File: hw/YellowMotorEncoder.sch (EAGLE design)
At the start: 20 parts, among them P1 M1

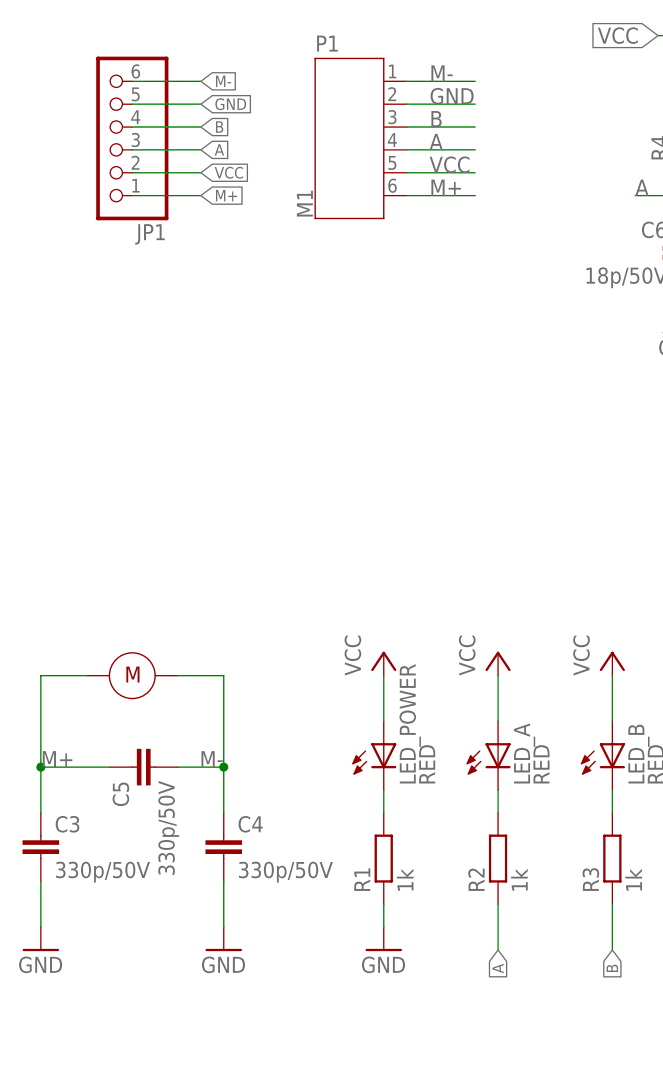
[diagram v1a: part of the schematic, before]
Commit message: Finish routing YellowMotorEncoder v1.0
- route PCB
- correct position of mounting holes
- fix connectors signal
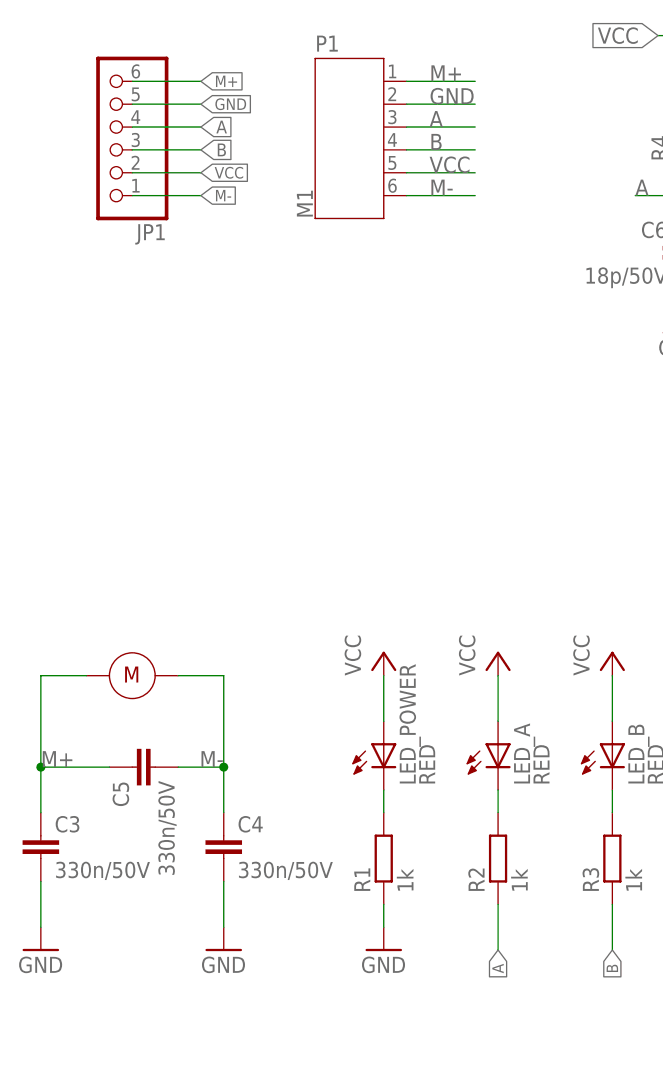
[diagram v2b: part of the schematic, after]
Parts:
- C3, C4, C5: value 330p/50V -> 330n/50V
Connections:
- net A: now also JP1.4, P1.3; no longer JP1.3, P1.4
- net B: now also JP1.3, P1.4; no longer JP1.4, P1.3
- net M+: now also JP1.6, P1.1, U$3.P$2; no longer JP1.1, P1.6, U$3.P$1
- net M-: now also JP1.1, P1.6, U$3.P$1; no longer JP1.6, P1.1, U$3.P$2
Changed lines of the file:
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@@
 <attribute name="PRICE_DATE" value="2020-05-08"/>
 </part>
-<part name="C3" library="rcl" deviceset="C-EU" device="C0805" value="330p/50V">
+<part name="C3" library="rcl" deviceset="C-EU" device="C0805" value="330n/50V">
 <attribute name="DESCRIPTION" value=" MULTILAYER CERAMIC CAPACITORS MLCC - SMD/SMT 330NF 50V 0805 ROHS"/>
 <attribute name="EXTENDED" value="NO"/>
@@
 <attribute name="PRICE_DATE" value="2020-05-08"/>
 </part>
-<part name="C4" library="rcl" deviceset="C-EU" device="C0805" value="330p/50V">
+<part name="C4" library="rcl" deviceset="C-EU" device="C0805" value="330n/50V">
 <attribute name="DESCRIPTION" value=" MULTILAYER CERAMIC CAPACITORS MLCC - SMD/SMT 330NF 50V 0805 ROHS"/>
 <attribute name="EXTENDED" value="NO"/>
@@
 <attribute name="PRICE_DATE" value="2020-05-08"/>
 </part>
-<part name="C5" library="rcl" deviceset="C-EU" device="C0805" value="330p/50V">
+<part name="C5" library="rcl" deviceset="C-EU" device="C0805" value="330n/50V">
 <attribute name="DESCRIPTION" value=" MULTILAYER CERAMIC CAPACITORS MLCC - SMD/SMT 330NF 50V 0805 ROHS"/>
 <attribute name="EXTENDED" value="NO"/>
@@
 <attribute name="EXTENDED" x="22.86" y="38.1" size="1.778" layer="96" rot="MR270" display="off"/>
 </instance>
-<instance part="U$3" gate="G$1" x="22.86" y="48.26" smashed="yes" rot="MR0"/>
+<instance part="U$3" gate="G$1" x="22.86" y="48.26" smashed="yes"/>
 </instances>
 <busses>
@@
 </segment>
 <segment>
-<wire x1="60.96" y1="111.76" x2="53.34" y2="111.76" width="0.1524" layer="91"/>
-<pinref part="P1" gate="A" pin="2"/>
-<label x="55.88" y="111.76" size="1.778" layer="95"/>
-</segment>
-<segment>
 <pinref part="JP1" gate="A" pin="5"/>
 <wire x1="22.86" y1="111.76" x2="30.48" y2="111.76" width="0.1524" layer="91"/>
 <label x="30.48" y="111.76" size="1.27" layer="95" xref="yes"/>
 </segment>
+<segment>
+<pinref part="P1" gate="A" pin="2"/>
+<wire x1="53.34" y1="111.76" x2="60.96" y2="111.76" width="0.1524" layer="91"/>
+<label x="55.88" y="111.76" size="1.778" layer="95"/>
+</segment>
 </net>
 <net name="B" class="0">
-<segment>
-<pinref part="JP1" gate="A" pin="4"/>
-<wire x1="22.86" y1="109.22" x2="30.48" y2="109.22" width="0.1524" layer="91"/>
-<label x="30.48" y="109.22" size="1.27" layer="95" xref="yes"/>
-</segment>
-<segment>
-<wire x1="53.34" y1="109.22" x2="60.96" y2="109.22" width="0.1524" layer="91"/>
-<pinref part="P1" gate="A" pin="3"/>
-<label x="55.88" y="109.22" size="1.778" layer="95"/>
-</segment>
 <segment>
 <wire x1="76.2" y1="22.86" x2="76.2" y2="17.78" width="0.1524" layer="91"/>
@@
 <pinref part="C7" gate="G$1" pin="1"/>
 </segment>
+<segment>
+<pinref part="P1" gate="A" pin="4"/>
+<wire x1="53.34" y1="106.68" x2="60.96" y2="106.68" width="0.1524" layer="91"/>
+<label x="55.88" y="106.68" size="1.778" layer="95"/>
+</segment>
+<segment>
+<pinref part="JP1" gate="A" pin="3"/>
+<wire x1="22.86" y1="106.68" x2="30.48" y2="106.68" width="0.1524" layer="91"/>
+<label x="30.48" y="106.68" size="1.4224" layer="95" xref="yes"/>
+</segment>
 </net>
 <net name="A" class="0">
-<segment>
-<pinref part="JP1" gate="A" pin="3"/>
-<wire x1="22.86" y1="106.68" x2="30.48" y2="106.68" width="0.1524" layer="91"/>
-<label x="30.48" y="106.68" size="1.27" layer="95" xref="yes"/>
-</segment>
-<segment>
-<wire x1="60.96" y1="106.68" x2="53.34" y2="106.68" width="0.1524" layer="91"/>
-<pinref part="P1" gate="A" pin="4"/>
-<label x="55.88" y="106.68" size="1.778" layer="95"/>
-</segment>
 <segment>
 <wire x1="63.5" y1="22.86" x2="63.5" y2="17.78" width="0.1524" layer="91"/>
@@
 <pinref part="R4" gate="G$1" pin="1"/>
 </segment>
+<segment>
+<pinref part="P1" gate="A" pin="3"/>
+<wire x1="53.34" y1="109.22" x2="60.96" y2="109.22" width="0.1524" layer="91"/>
+<label x="55.88" y="109.22" size="1.778" layer="95"/>
+</segment>
+<segment>
+<pinref part="JP1" gate="A" pin="4"/>
+<wire x1="22.86" y1="109.22" x2="30.48" y2="109.22" width="0.1524" layer="91"/>
+<label x="30.48" y="109.22" size="1.4224" layer="95" xref="yes"/>
+</segment>
 </net>
 <net name="M-" class="0">
@@
 <pinref part="C4" gate="G$1" pin="1"/>
 <pinref part="C5" gate="G$1" pin="2"/>
-<pinref part="U$3" gate="G$1" pin="P$2"/>
+<pinref part="U$3" gate="G$1" pin="P$1"/>
 <wire x1="27.94" y1="48.26" x2="33.02" y2="48.26" width="0.1524" layer="91"/>
 </segment>
 <segment>
-<pinref part="JP1" gate="A" pin="6"/>
-<wire x1="22.86" y1="114.3" x2="30.48" y2="114.3" width="0.1524" layer="91"/>
-<label x="30.48" y="114.3" size="1.27" layer="95" xref="yes"/>
-</segment>
-<segment>
-<wire x1="53.34" y1="114.3" x2="60.96" y2="114.3" width="0.1524" layer="91"/>
-<pinref part="P1" gate="A" pin="1"/>
-<label x="55.88" y="114.3" size="1.778" layer="95"/>
+<wire x1="53.34" y1="101.6" x2="60.96" y2="101.6" width="0.1524" layer="91"/>
+<pinref part="P1" gate="A" pin="6"/>
+<label x="55.88" y="101.6" size="1.778" layer="95"/>
+</segment>
+<segment>
+<pinref part="JP1" gate="A" pin="1"/>
+<wire x1="22.86" y1="101.6" x2="30.48" y2="101.6" width="0.1524" layer="91"/>
+<label x="30.48" y="101.6" size="1.27" layer="95" xref="yes"/>
 </segment>
 </net>
@@
 <pinref part="C3" gate="G$1" pin="1"/>
 <pinref part="C5" gate="G$1" pin="1"/>
-<pinref part="U$3" gate="G$1" pin="P$1"/>
-<wire x1="12.7" y1="48.26" x2="17.78" y2="48.26" width="0.1524" layer="91"/>
-</segment>
-<segment>
-<pinref part="JP1" gate="A" pin="1"/>
-<wire x1="22.86" y1="101.6" x2="30.48" y2="101.6" width="0.1524" layer="91"/>
-<label x="30.48" y="101.6" size="1.27" layer="95" xref="yes"/>
-</segment>
-<segment>
-<wire x1="53.34" y1="101.6" x2="60.96" y2="101.6" width="0.1524" layer="91"/>
-<pinref part="P1" gate="A" pin="6"/>
-<label x="55.88" y="101.6" size="1.778" layer="95"/>
+<pinref part="U$3" gate="G$1" pin="P$2"/>
+<wire x1="17.78" y1="48.26" x2="12.7" y2="48.26" width="0.1524" layer="91"/>
+</segment>
+<segment>
+<wire x1="53.34" y1="114.3" x2="60.96" y2="114.3" width="0.1524" layer="91"/>
+<pinref part="P1" gate="A" pin="1"/>
+<label x="55.88" y="114.3" size="1.778" layer="95"/>
+</segment>
+<segment>
+<pinref part="JP1" gate="A" pin="6"/>
+<wire x1="22.86" y1="114.3" x2="30.48" y2="114.3" width="0.1524" layer="91"/>
+<label x="30.48" y="114.3" size="1.27" layer="95" xref="yes"/>
 </segment>
 </net>
@@
 </segment>
 <segment>
-<wire x1="60.96" y1="104.14" x2="53.34" y2="104.14" width="0.1524" layer="91"/>
-<pinref part="P1" gate="A" pin="5"/>
-<label x="55.88" y="104.14" size="1.778" layer="95"/>
-</segment>
-<segment>
 <pinref part="JP1" gate="A" pin="2"/>
 <wire x1="22.86" y1="104.14" x2="30.48" y2="104.14" width="0.1524" layer="91"/>
@@
 <pinref part="LED_B" gate="G$1" pin="A"/>
 </segment>
+<segment>
+<pinref part="P1" gate="A" pin="5"/>
+<wire x1="53.34" y1="104.14" x2="60.96" y2="104.14" width="0.1524" layer="91"/>
+<label x="55.88" y="104.14" size="1.778" layer="95"/>
+</segment>
 </net>

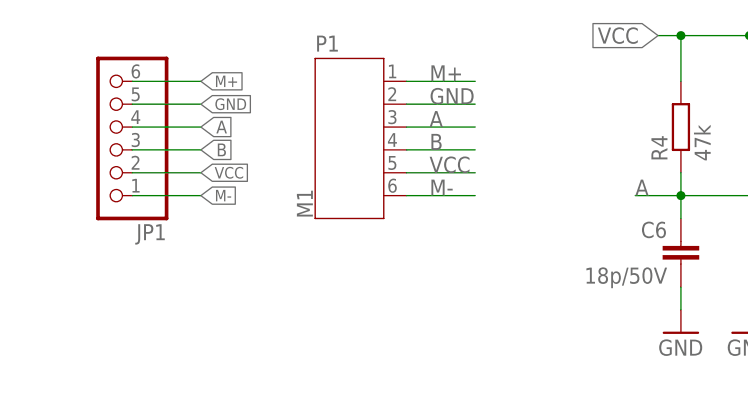
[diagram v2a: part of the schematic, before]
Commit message: Swap encoder power polarity
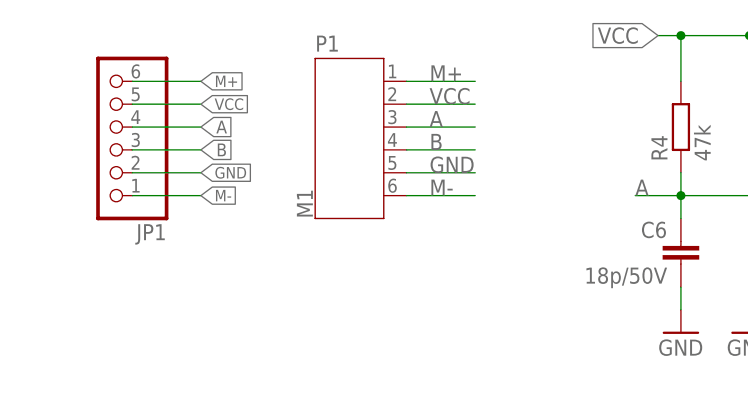
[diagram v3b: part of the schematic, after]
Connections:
- net GND: now also JP1.2, P1.5; no longer JP1.5, P1.2
- net VCC: now also JP1.5, P1.2; no longer JP1.2, P1.5
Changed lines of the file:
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@@
 <?xml version="1.0" encoding="utf-8"?>
 <!DOCTYPE eagle SYSTEM "eagle.dtd">
-<eagle version="9.6.0">
+<eagle version="9.6.1">
 <drawing>
 <settings>
@@
 </segment>
 <segment>
-<pinref part="JP1" gate="A" pin="5"/>
-<wire x1="22.86" y1="111.76" x2="30.48" y2="111.76" width="0.1524" layer="91"/>
-<label x="30.48" y="111.76" size="1.27" layer="95" xref="yes"/>
-</segment>
-<segment>
-<pinref part="P1" gate="A" pin="2"/>
-<wire x1="53.34" y1="111.76" x2="60.96" y2="111.76" width="0.1524" layer="91"/>
-<label x="55.88" y="111.76" size="1.778" layer="95"/>
+<pinref part="P1" gate="A" pin="5"/>
+<wire x1="53.34" y1="104.14" x2="60.96" y2="104.14" width="0.1524" layer="91"/>
+<label x="55.88" y="104.14" size="1.778" layer="95"/>
+</segment>
+<segment>
+<pinref part="JP1" gate="A" pin="2"/>
+<wire x1="22.86" y1="104.14" x2="30.48" y2="104.14" width="0.1524" layer="91"/>
+<label x="30.48" y="104.14" size="1.27" layer="95" xref="yes"/>
 </segment>
 </net>
@@
 </segment>
 <segment>
-<pinref part="JP1" gate="A" pin="2"/>
-<wire x1="22.86" y1="104.14" x2="30.48" y2="104.14" width="0.1524" layer="91"/>
-<label x="30.48" y="104.14" size="1.27" layer="95" xref="yes"/>
-</segment>
-<segment>
 <pinref part="LED_POWER" gate="G$1" pin="A"/>
 <wire x1="50.8" y1="48.26" x2="50.8" y2="43.18" width="0.1524" layer="91"/>
@@
 </segment>
 <segment>
-<pinref part="P1" gate="A" pin="5"/>
-<wire x1="53.34" y1="104.14" x2="60.96" y2="104.14" width="0.1524" layer="91"/>
-<label x="55.88" y="104.14" size="1.778" layer="95"/>
+<pinref part="P1" gate="A" pin="2"/>
+<wire x1="53.34" y1="111.76" x2="60.96" y2="111.76" width="0.1524" layer="91"/>
+<label x="55.88" y="111.76" size="1.778" layer="95"/>
+</segment>
+<segment>
+<pinref part="JP1" gate="A" pin="5"/>
+<wire x1="22.86" y1="111.76" x2="30.48" y2="111.76" width="0.1524" layer="91"/>
+<label x="30.48" y="111.76" size="1.27" layer="95" xref="yes"/>
 </segment>
 </net>

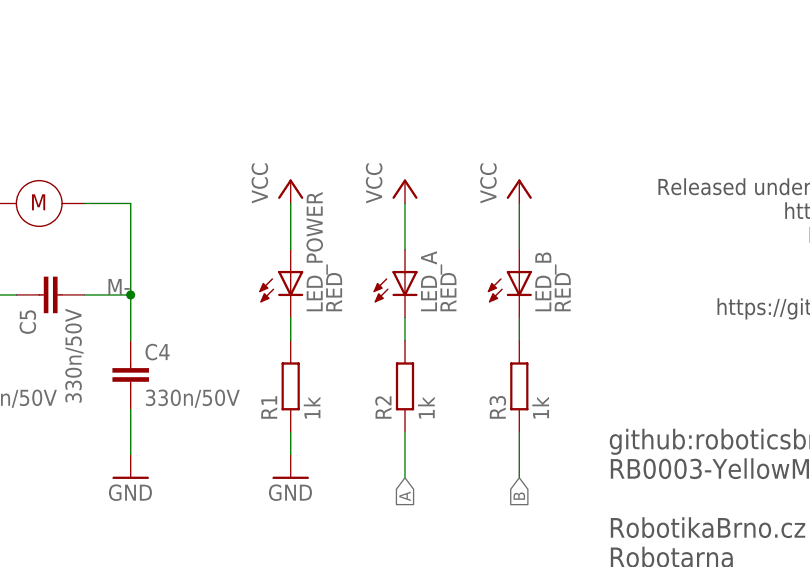
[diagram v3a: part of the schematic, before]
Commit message: Fixed LEDs orientation
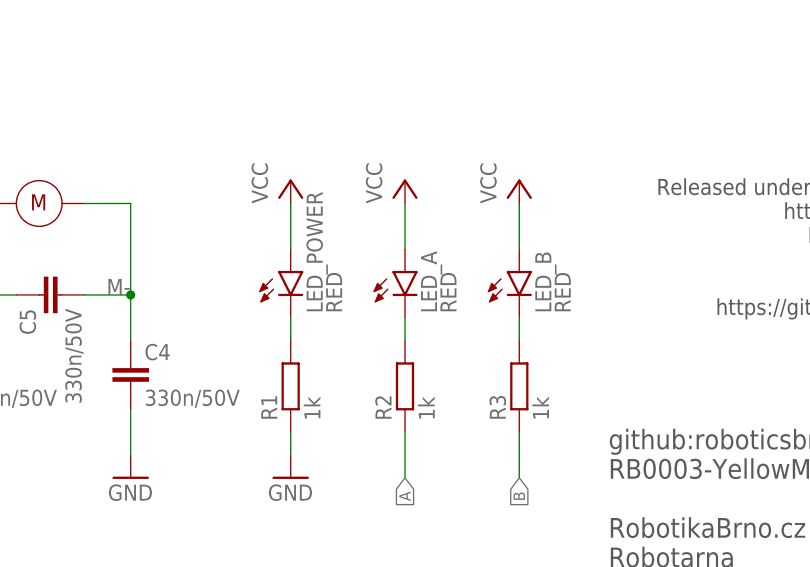
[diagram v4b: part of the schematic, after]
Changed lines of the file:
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@@
 <attribute name="PRICE_DATE" value="2020-05-08"/>
 </part>
-<part name="LED_POWER" library="led" library_urn="urn:adsk.eagle:library:259" deviceset="LED" device="CHIPLED_0603" package3d_urn="urn:adsk.eagle:package:15822/2" value="RED">
+<part name="LED_POWER" library="led" deviceset="LED" device="CHIPLED_0603" package3d_urn="urn:adsk.eagle:package:15822/2" value="RED">
 <attribute name="DESCRIPTION" value="LIGHT EMITTING DIODES (LED) RED 520~625NM 90~100MCD@20MA TOP VIEW 0603 ROHS"/>
 <attribute name="DIGIKEY" value="160-1446-1-ND"/>
@@
 <part name="U$1" library="hall_sensor" deviceset="MH253ESO" device="" package3d_urn="urn:adsk.eagle:package:43389/2"/>
 <part name="U$2" library="hall_sensor" deviceset="MH253ESO" device="" package3d_urn="urn:adsk.eagle:package:43389/2"/>
-<part name="LED_A" library="led" library_urn="urn:adsk.eagle:library:259" deviceset="LED" device="CHIPLED_0603" package3d_urn="urn:adsk.eagle:package:15822/2" value="RED">
+<part name="LED_A" library="led" deviceset="LED" device="CHIPLED_0603" package3d_urn="urn:adsk.eagle:package:15822/2" value="RED">
 <attribute name="DESCRIPTION" value="LIGHT EMITTING DIODES (LED) RED 520~625NM 90~100MCD@20MA TOP VIEW 0603 ROHS"/>
 <attribute name="DIGIKEY" value="160-1446-1-ND"/>
@@
 <attribute name="RS" value="872-1799"/>
 </part>
-<part name="LED_B" library="led" library_urn="urn:adsk.eagle:library:259" deviceset="LED" device="CHIPLED_0603" package3d_urn="urn:adsk.eagle:package:15822/2" value="RED">
+<part name="LED_B" library="led" deviceset="LED" device="CHIPLED_0603" package3d_urn="urn:adsk.eagle:package:15822/2" value="RED">
 <attribute name="DESCRIPTION" value="LIGHT EMITTING DIODES (LED) RED 520~625NM 90~100MCD@20MA TOP VIEW 0603 ROHS"/>
 <attribute name="DIGIKEY" value="160-1446-1-ND"/>
